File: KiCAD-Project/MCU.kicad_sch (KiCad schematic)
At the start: 35 parts, among them J301 GPIOs, J302 JTAG/SWD, J303 Conn_01x03_Shielded, U301 CY8C6244AZI-S4D92, U302 MCP9700AT-HTT, Y301 32MHz

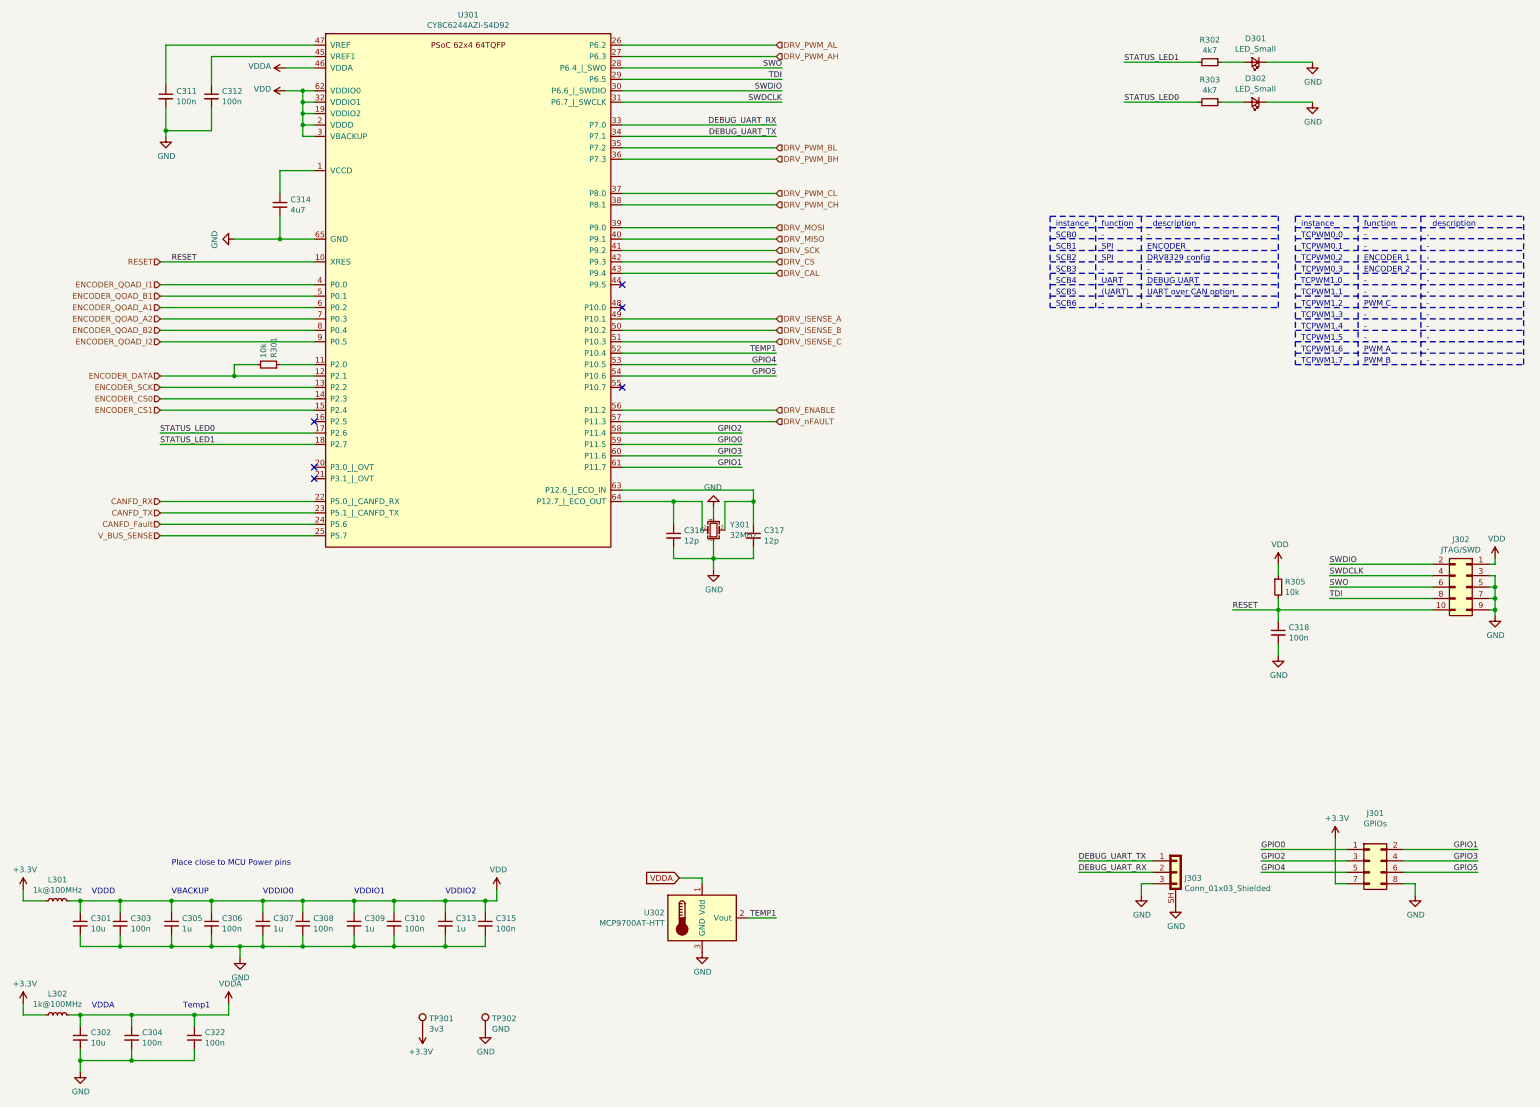
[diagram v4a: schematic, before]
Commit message: changed connectors to THT
changed connectors to THT, removed UART connector
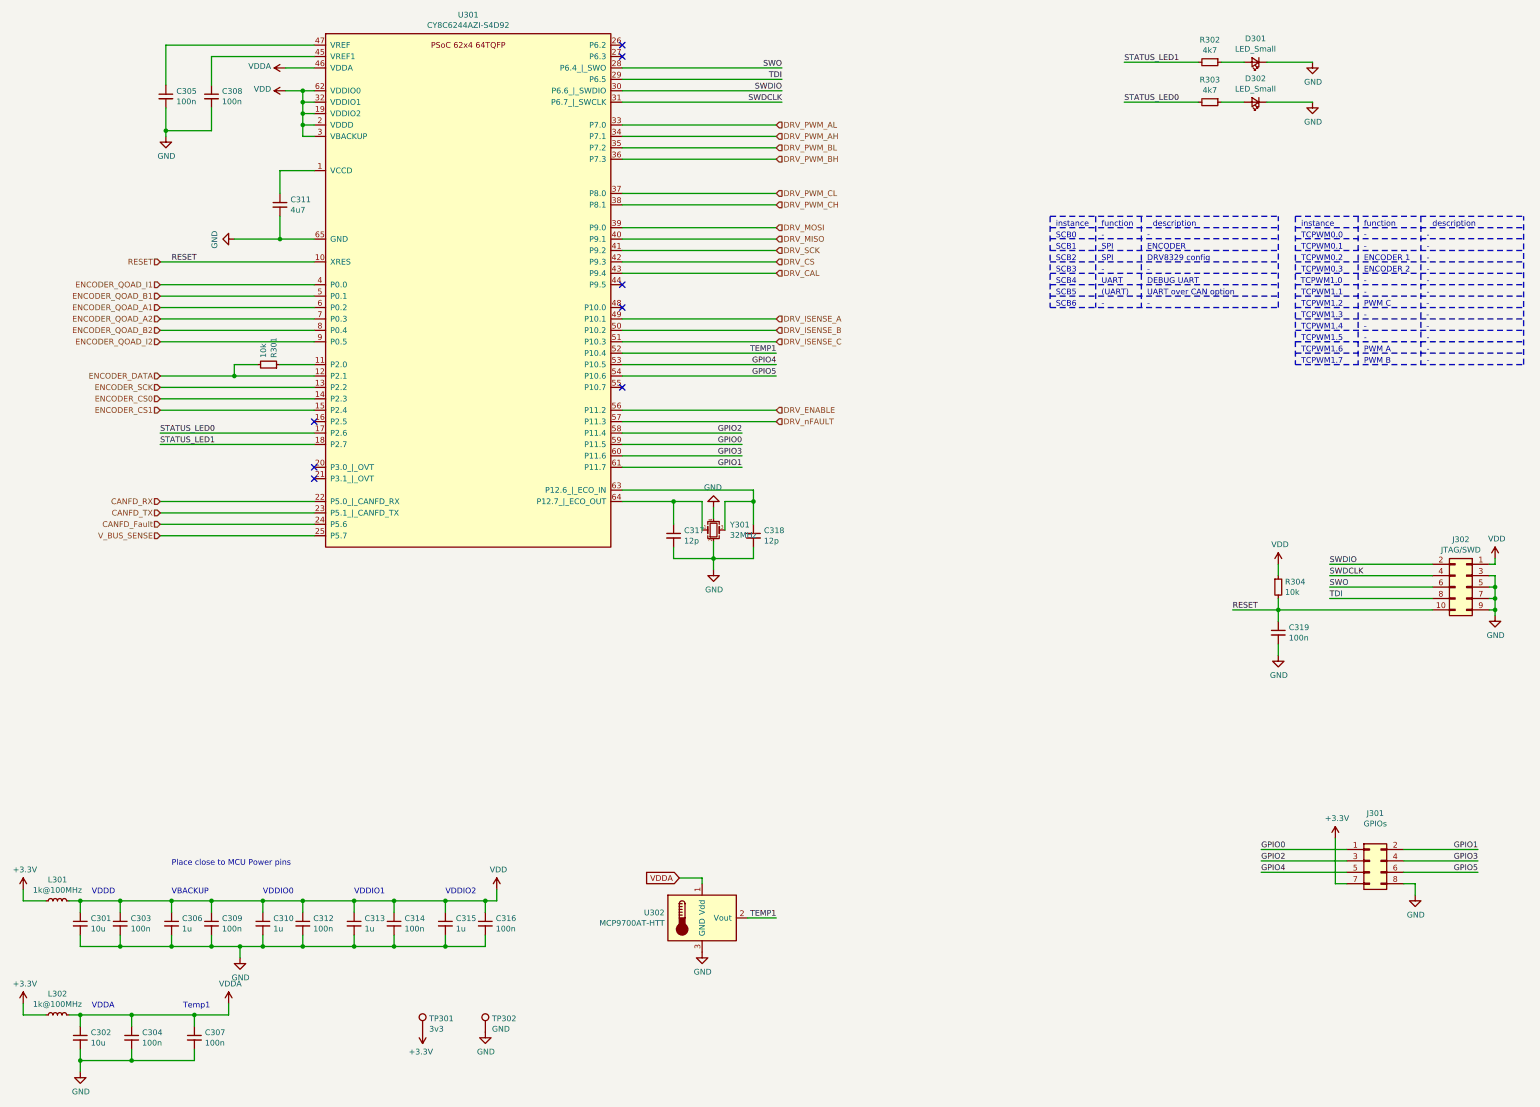
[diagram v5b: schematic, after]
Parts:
- removed J303: Conn_01x03_Shielded, Connector_JST:JST_PH_S3B-PH-SM4-TB_1x03-1MP_P2.00mm_Horizontal, symbol Connector_Generic_Shielded:Conn_01x03_Shielded
- J301: footprint Connector_PinHeader_2.54mm:PinHeader_2x04_P2.54mm_Vertical_SMD -> Connector_PinHeader_2.54mm:PinHeader_2x04_P2.54mm_Vertical
- renumbered C311 to C305, C305 to C306, C322 to C307, C312 to C308, C306 to C309, C307 to C310, C314 to C311, C308 to C312, C309 to C313, C310 to C314, C313 to C315, C315 to C316, C316 to C317, C317 to C318, C318 to C319, R305 to R304
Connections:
- net DEBUG_UART_RX is gone; now on net DRV_PWM_AL: U301.33 (P7.0)
- net DEBUG_UART_TX is gone; now on net DRV_PWM_AH: U301.34 (P7.1)
- net DRV_PWM_AH: no longer U301.27 (P6.3)
- net DRV_PWM_AL: no longer U301.26 (P6.2)
- no-connect marks 6 -> 8

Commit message: minor pcb updates
swapped Encoder Quadrature signals, to provide debug UART
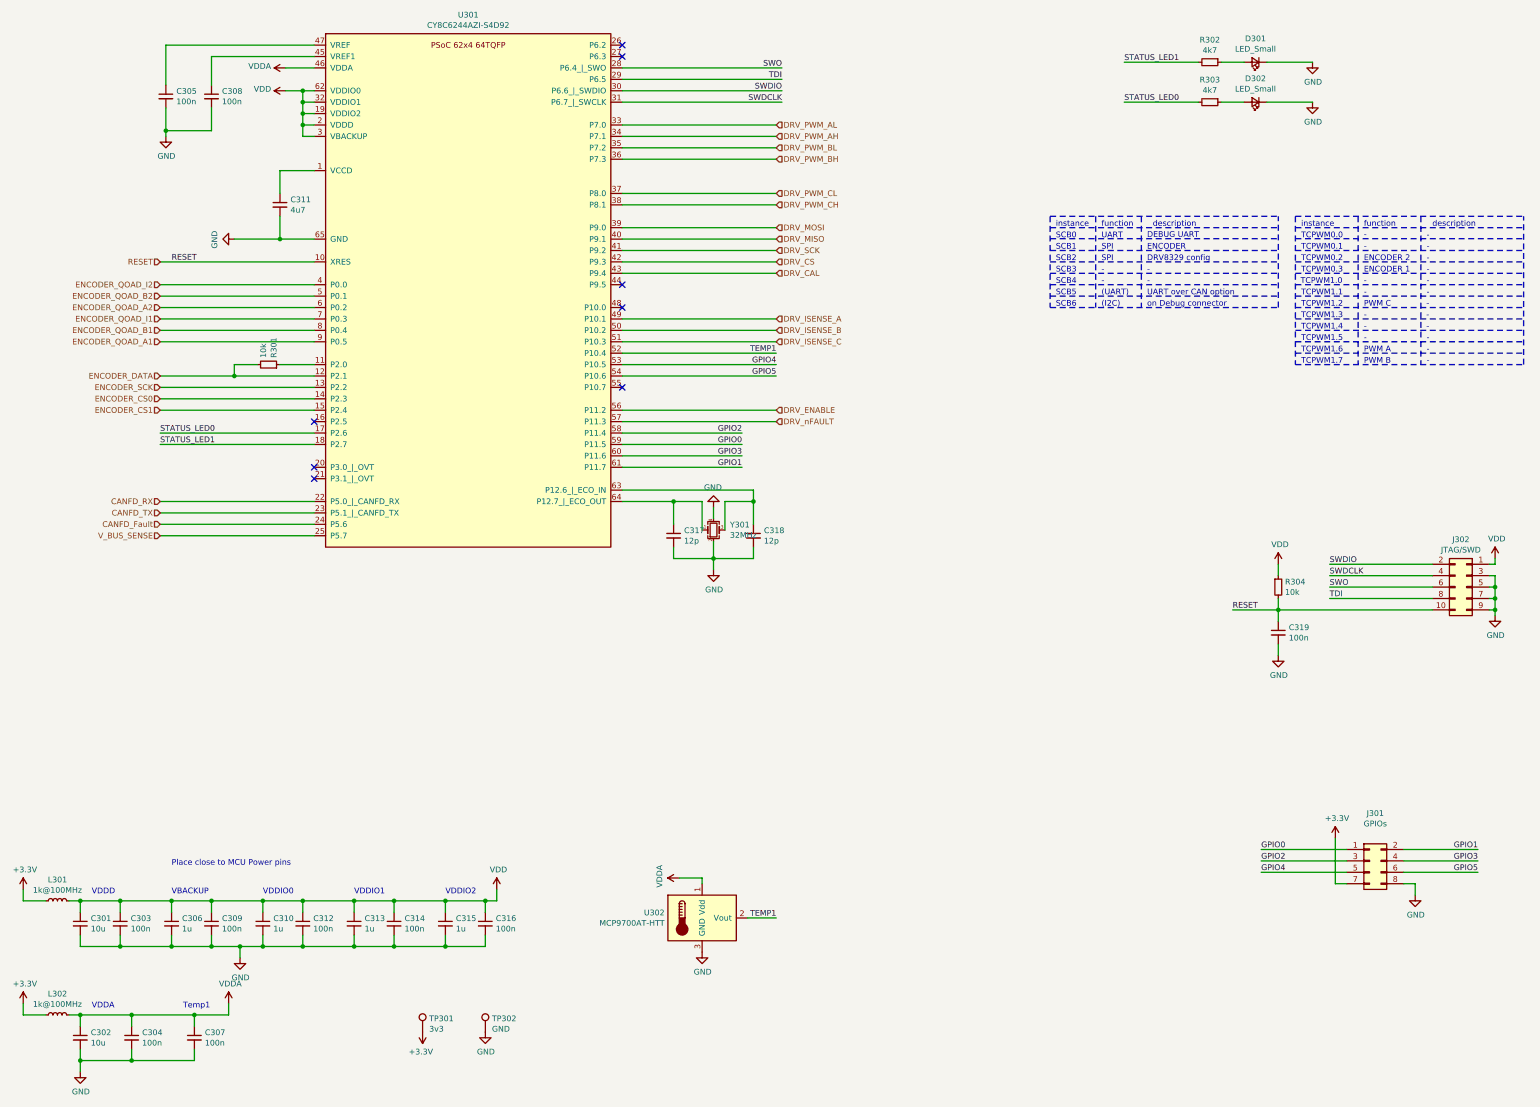
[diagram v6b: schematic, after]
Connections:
- net ENCODER_QOAD_A1: now also U301.9 (P0.5); no longer U301.6 (P0.2)
- net ENCODER_QOAD_A2: now also U301.6 (P0.2); no longer U301.7 (P0.3)
- net ENCODER_QOAD_B1: now also U301.8 (P0.4); no longer U301.5 (P0.1)
- net ENCODER_QOAD_B2: now also U301.5 (P0.1); no longer U301.8 (P0.4)
- net ENCODER_QOAD_I1: now also U301.7 (P0.3); no longer U301.4 (P0.0)
- net ENCODER_QOAD_I2: now also U301.4 (P0.0); no longer U301.9 (P0.5)
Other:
- note added: "(I2C)"
- note added: "on Debug connector"
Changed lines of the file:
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@@
     (effects (font (size 1.27 1.27)) (justify left bottom))
   )
-  (text "-" (at 265.43 68.58 0)
+  (text "UART" (at 265.43 68.58 0)
     (effects (font (size 1.27 1.27)) (justify left bottom))
   )
@@
     (effects (font (size 1.27 1.27)) (justify left bottom))
   )
-  (text "UART" (at 265.43 78.74 0)
+  (text "-" (at 265.43 78.74 0)
     (effects (font (size 1.27 1.27)) (justify left bottom))
   )
@@
     (effects (font (size 1.27 1.27)) (justify left bottom))
   )
-  (text "-" (at 265.43 83.82 0)
-    (effects (font (size 1.27 1.27)) (justify left bottom))
-  )
-  (text "-" (at 275.59 68.4936 0)
+  (text "(I2C)" (at 265.43 83.82 0)
+    (effects (font (size 1.27 1.27)) (justify left bottom))
+  )
+  (text "DEBUG UART" (at 275.59 68.4936 0)
     (effects (font (size 1.27 1.27)) (justify left bottom))
   )
@@
     (effects (font (size 1.27 1.27)) (justify left bottom))
   )
-  (text "DEBUG UART" (at 275.59 78.74 0)
+  (text "-" (at 275.59 78.74 0)
     (effects (font (size 1.27 1.27)) (justify left bottom))
   )
@@
     (effects (font (size 1.27 1.27)) (justify left bottom))
   )
-  (text "-" (at 275.59 83.82 0)
+  (text "on Debug connector" (at 275.59 83.82 0)
     (effects (font (size 1.27 1.27)) (justify left bottom))
   )
@@
     (effects (font (size 1.27 1.27)) (justify left bottom))
   )
-  (text "ENCODER 1" (at 323.85 73.66 0)
-    (effects (font (size 1.27 1.27)) (justify left bottom))
-  )
-  (text "ENCODER 2" (at 323.85 76.2 0)
+  (text "ENCODER 2" (at 323.85 73.66 0)
+    (effects (font (size 1.27 1.27)) (justify left bottom))
+  )
+  (text "ENCODER 1" (at 323.85 76.2 0)
     (effects (font (size 1.27 1.27)) (justify left bottom))
   )
@@
     (effects (font (size 1.27 1.27)) (justify right bottom))
   )
-  (global_label "VDDA" (shape input) (at 171.45 210.82 180) (fields_autoplaced)
-    (effects (font (size 1.27 1.27)) (justify right))
-    (property "Intersheet References" "${INTERSHEET_REFS}" (id 0) (at 0 0 0)
-      (effects (font (size 1.27 1.27)) hide)
-    )
-  )
   (hierarchical_label "RESET" (shape input) (at 55.88 73.66 180)
     (effects (font (size 1.27 1.27)) (justify right))
   )
-  (hierarchical_label "ENCODER_QOAD_I1" (shape input) (at 55.88 78.74 180)
-    (effects (font (size 1.27 1.27)) (justify right))
-  )
-  (hierarchical_label "ENCODER_QOAD_B1" (shape input) (at 55.88 81.28 180)
-    (effects (font (size 1.27 1.27)) (justify right))
-  )
-  (hierarchical_label "ENCODER_QOAD_A1" (shape input) (at 55.88 83.82 180)
-    (effects (font (size 1.27 1.27)) (justify right))
-  )
-  (hierarchical_label "ENCODER_QOAD_A2" (shape input) (at 55.88 86.36 180)
-    (effects (font (size 1.27 1.27)) (justify right))
-  )
-  (hierarchical_label "ENCODER_QOAD_B2" (shape input) (at 55.88 88.9 180)
-    (effects (font (size 1.27 1.27)) (justify right))
-  )
-  (hierarchical_label "ENCODER_QOAD_I2" (shape input) (at 55.88 91.44 180)
+  (hierarchical_label "ENCODER_QOAD_I2" (shape input) (at 55.88 78.74 180)
+    (effects (font (size 1.27 1.27)) (justify right))
+  )
+  (hierarchical_label "ENCODER_QOAD_B2" (shape input) (at 55.88 81.28 180)
+    (effects (font (size 1.27 1.27)) (justify right))
+  )
+  (hierarchical_label "ENCODER_QOAD_A2" (shape input) (at 55.88 83.82 180)
+    (effects (font (size 1.27 1.27)) (justify right))
+  )
+  (hierarchical_label "ENCODER_QOAD_I1" (shape input) (at 55.88 86.36 180)
+    (effects (font (size 1.27 1.27)) (justify right))
+  )
+  (hierarchical_label "ENCODER_QOAD_B1" (shape input) (at 55.88 88.9 180)
+    (effects (font (size 1.27 1.27)) (justify right))
+  )
+  (hierarchical_label "ENCODER_QOAD_A1" (shape input) (at 55.88 91.44 180)
     (effects (font (size 1.27 1.27)) (justify right))
   )
@@
       (effects (font (size 1.27 1.27)) hide)
     )
+    (pin "1")
+  )
+  (symbol (lib_id "power:VDDA") (at 171.45 210.82 90) (unit 1)
+    (in_bom yes) (on_board yes)
+    (property "Reference" "#PWR0101" (id 0) (at 175.26 210.82 0)
+      (effects (font (size 1.27 1.27)) hide)
+    )
+    (property "Value" "VDDA" (id 1) (at 167.0558 210.439 0))
+    (property "Footprint" "" (id 2) (at 171.45 210.82 0)
+      (effects (font (size 1.27 1.27)) hide)
+    )
+    (property "Datasheet" "" (id 3) (at 171.45 210.82 0)
+      (effects (font (size 1.27 1.27)) hide)
+    )
